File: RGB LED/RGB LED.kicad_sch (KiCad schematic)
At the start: 0 parts

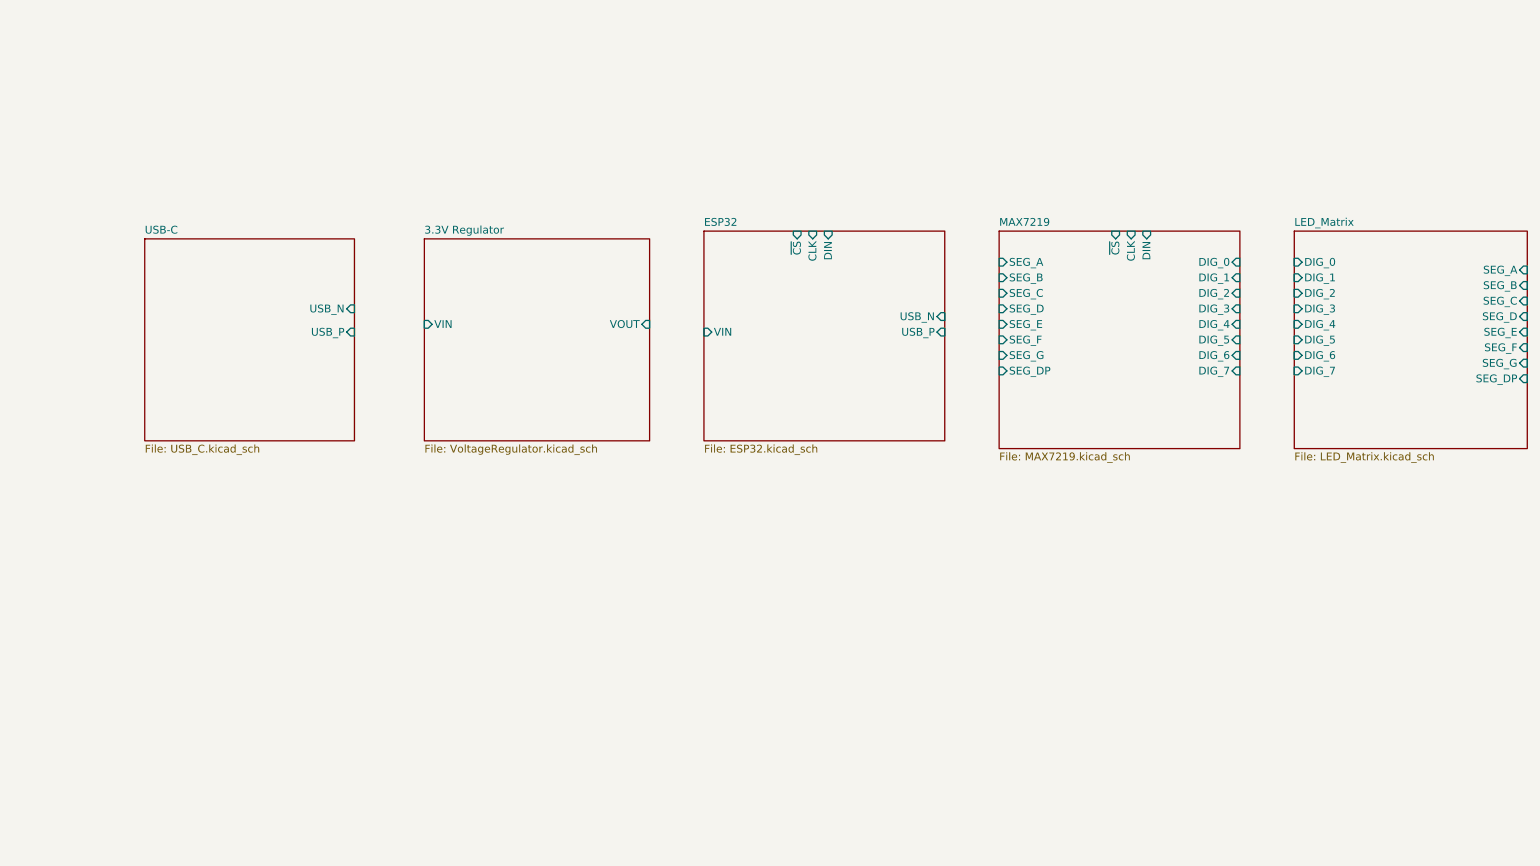
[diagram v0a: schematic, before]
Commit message: edited according to feedback
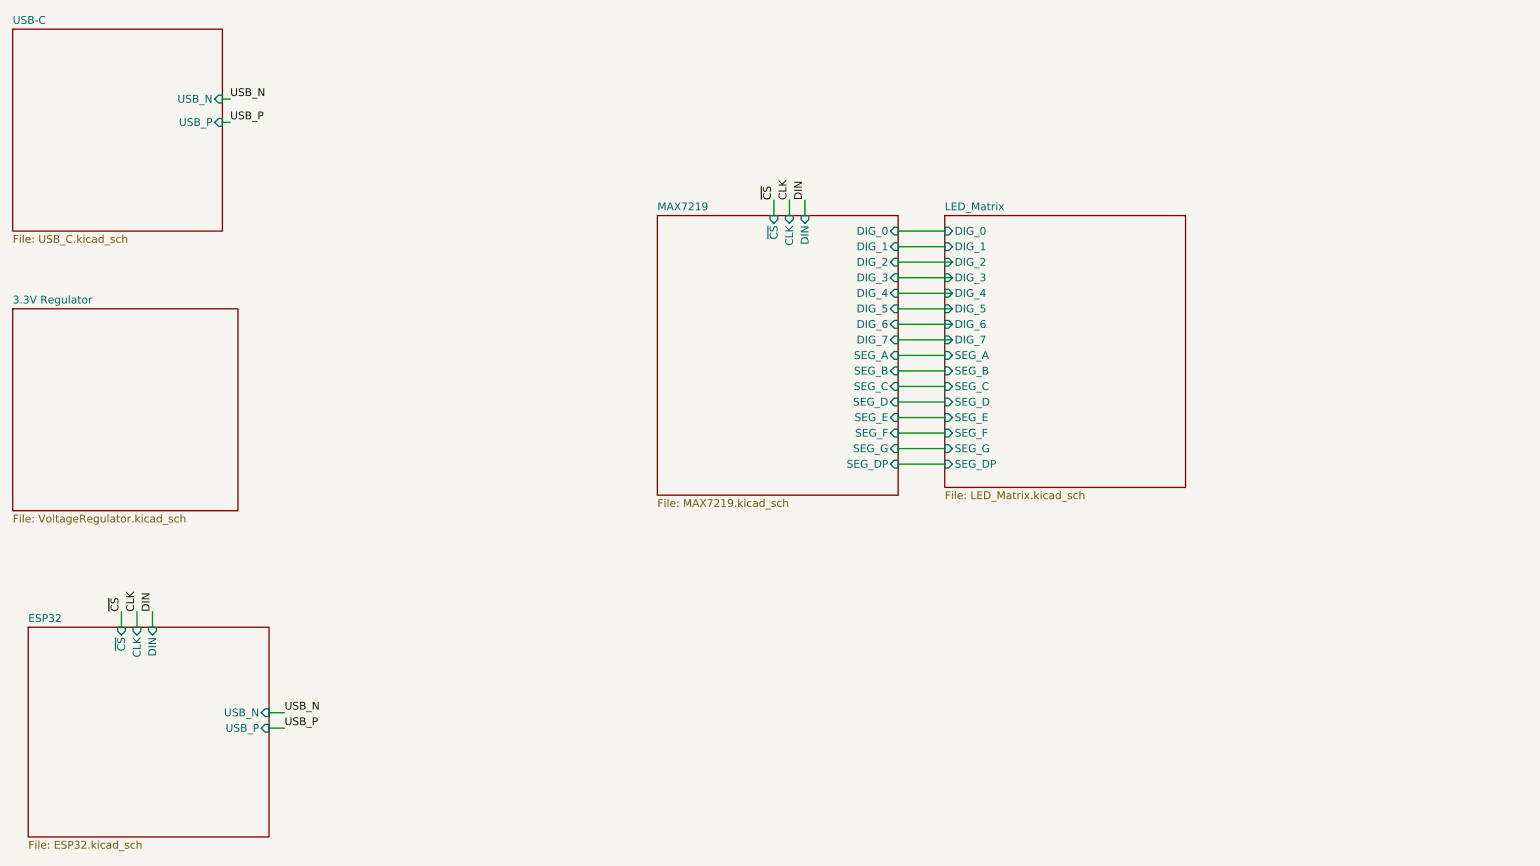
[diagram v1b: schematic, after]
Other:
- sheet 3.3V Regulator ports: added none; removed VIN, VOUT
- sheet ESP32 ports: added none; removed VIN

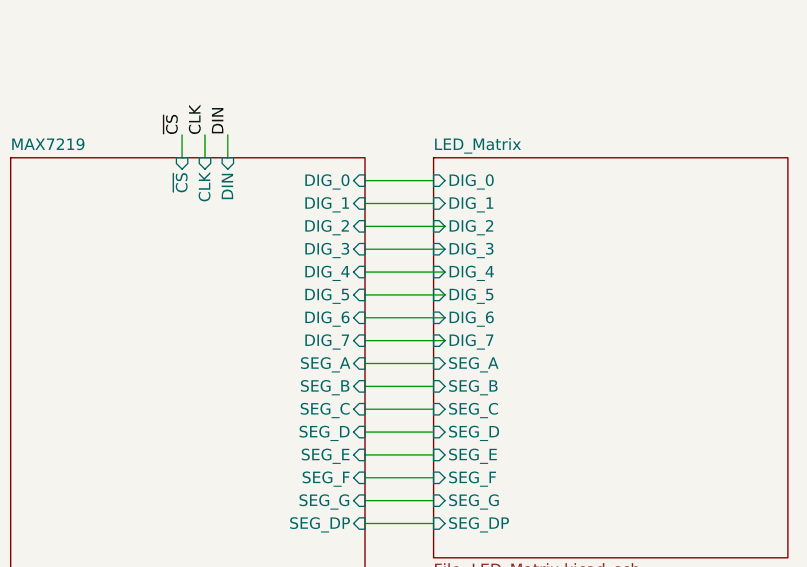
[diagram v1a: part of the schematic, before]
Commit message: changed layout, added traces/vias
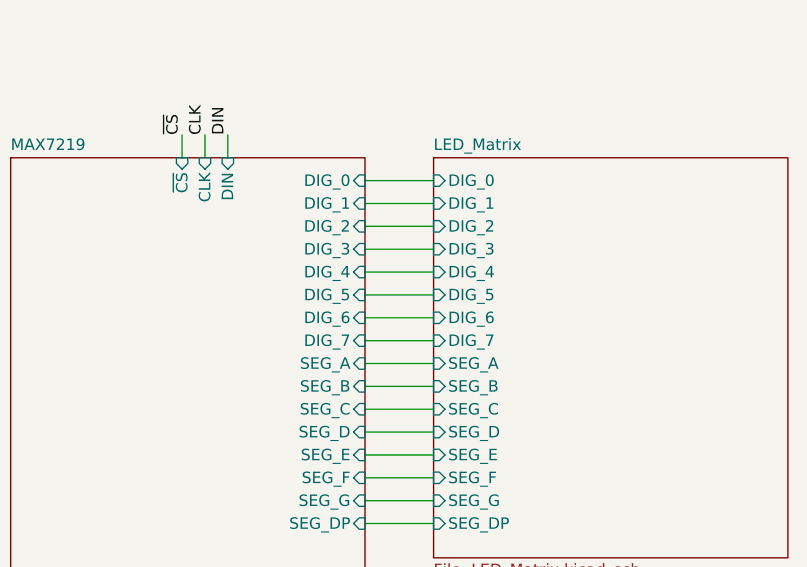
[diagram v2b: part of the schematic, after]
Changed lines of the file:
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@@
-    (stroke (width 0) (type default))
-  )
-  (wire (pts (xy 166.37 72.39) (xy 175.26 72.39))
     (stroke (width 0) (type default))
   )
@@
     (stroke (width 0) (type default))
   )
-  (wire (pts (xy 166.37 74.93) (xy 175.26 74.93))
+  (wire (pts (xy 166.37 67.31) (xy 173.99 67.31))
     (stroke (width 0) (type default))
   )
-  (wire (pts (xy 166.37 64.77) (xy 175.26 64.77))
+  (wire (pts (xy 166.37 69.85) (xy 173.99 69.85))
+    (stroke (width 0) (type default))
+  )
+  (wire (pts (xy 166.37 74.93) (xy 173.99 74.93))
+    (stroke (width 0) (type default))
+  )
+  (wire (pts (xy 166.37 72.39) (xy 173.99 72.39))
+    (stroke (width 0) (type default))
+  )
+  (wire (pts (xy 166.37 64.77) (xy 173.99 64.77))
     (stroke (width 0) (type default))
   )
   (wire (pts (xy 55.88 39.37) (xy 57.15 39.37))
-    (stroke (width 0) (type default))
-  )
-  (wire (pts (xy 166.37 69.85) (xy 175.26 69.85))
-    (stroke (width 0) (type default))
-  )
-  (wire (pts (xy 166.37 62.23) (xy 175.26 62.23))
     (stroke (width 0) (type default))
   )
@@
     (stroke (width 0) (type default))
   )
+  (wire (pts (xy 166.37 62.23) (xy 173.99 62.23))
+    (stroke (width 0) (type default))
+  )
   (wire (pts (xy 146.05 52.07) (xy 146.05 54.61))
     (stroke (width 0) (type default))
@@
     (stroke (width 0) (type default))
   )
-  (wire (pts (xy 166.37 67.31) (xy 175.26 67.31))
-    (stroke (width 0) (type default))
-  )
